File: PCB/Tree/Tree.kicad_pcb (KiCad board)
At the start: 2 copper layers, 70 x 98 mm, 36 parts, among them U1 HT16K33-28SOP

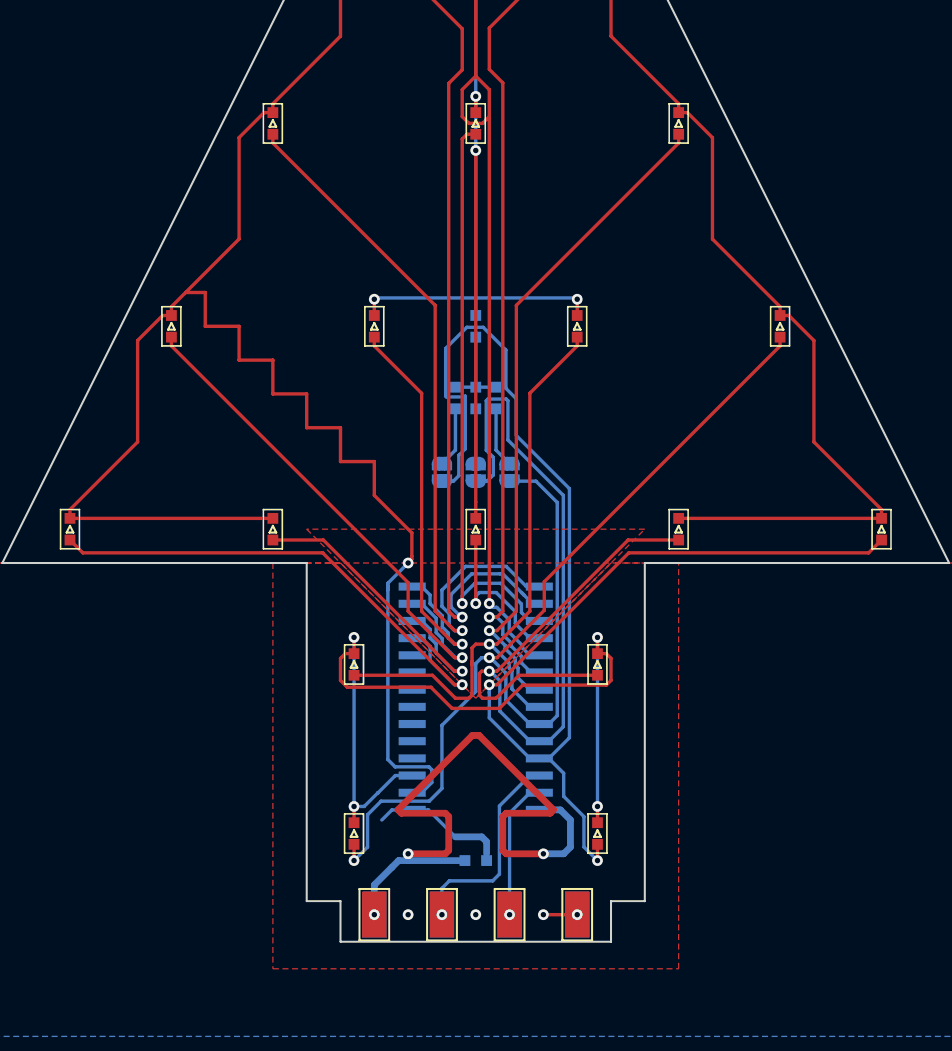
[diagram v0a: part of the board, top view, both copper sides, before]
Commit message: [update] Treeのコネクタ変更に伴う外形検討前 #2
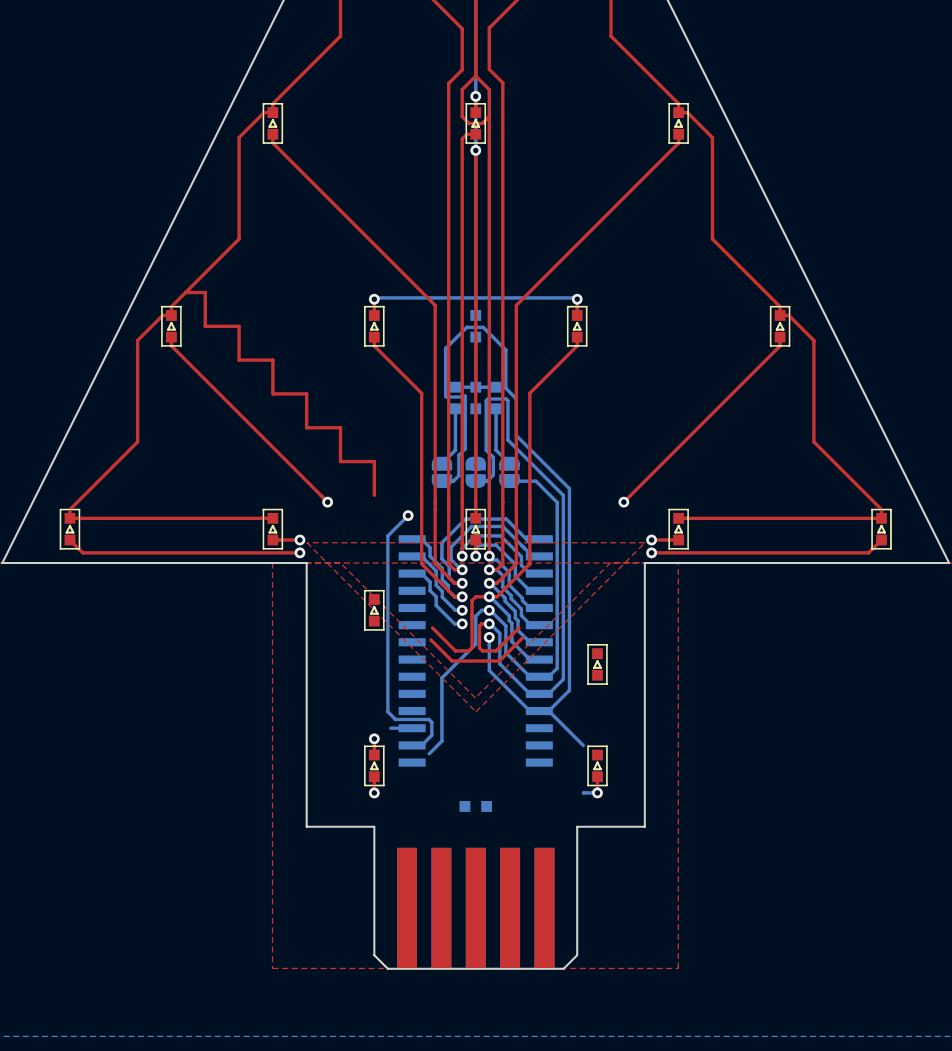
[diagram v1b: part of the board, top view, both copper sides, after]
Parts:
- removed TP1, TP2, TP3, TP4, TP5, TP6, TP7, TP8: TestPoint, TestPoint:TestPoint_Keystone_5015_Micro-Minature
- added J1: Conn_01x05, extsui:EDAC_5P_P2.54mm, F.Cu at (130.0, 150.5)
- D1, D10, D11, D12, D13, D14, D15, D16, D17, D18, D19, D2, D3, D4, D5, D6, D7, D8, D9: value GLED -> LED
- moved D18 5.22 mm to (122.5, 140.0)
- moved D16 5.00 mm to (139.0, 140.0)
- moved D19 4.27 mm to (122.5, 128.5)
- moved C1 4.00 mm to (130.0, 143.0)
- moved U1 3.50 mm to (130.0, 131.5)
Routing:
- net +5V: track 52.1 -> 0.00 mm, vias 3 -> 0
- net Net-(D16-Pad1): track 62.3 -> 10.9 mm, vias 4 -> 1
- net Net-(D18-Pad2): track 84.1 -> 55.9 mm, vias 2 -> 3
- net Net-(D17-Pad2): track 74.0 -> 48.7 mm, vias 1 -> 2
- net Net-(D1-Pad2): track 103.6 -> 79.7 mm, vias 2 -> 3
- net Net-(D15-Pad2): track 39.2 -> 17.4 mm
- net Net-(D14-Pad2): track 24.0 -> 7.99 mm, vias 1 -> 2
- net SCL: track 15.6 -> 0.00 mm, vias 1 -> 0
- net Net-(D13-Pad2): track 39.2 -> 23.9 mm, vias 1 -> 2
- net GND: track 12.4 -> 0.00 mm, vias 4 -> 0
- net SDA: track 11.3 -> 0.00 mm, vias 1 -> 0
- net Net-(D19-Pad2): track 47.0 -> 37.7 mm
- net Net-(D1-Pad1): track 328.2 -> 320.9 mm
- net Net-(D7-Pad2): track 76.7 -> 73.2 mm
- net Net-(D12-Pad2): track 32.3 -> 28.8 mm
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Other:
- board size 70 x 98 mm -> 70 x 100 mm
- board text removed: "GND"
- board text removed: "SCL"
- board text removed: "SDA"
- board text removed: "VCC"

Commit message: [update] Treeのコネクタ変更完了 #2
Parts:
- moved C1 4.61 mm to (125.5, 142.0), turned to 180 degrees
- moved D1 4.47 mm to (158.0, 118.5)
- moved D15 4.47 mm to (102.0, 118.5)
- moved D17 4.27 mm to (137.5, 128.5), turned to 90 degrees
- moved D14 4.00 mm to (115.0, 118.5)
- moved D2 4.00 mm to (145.0, 118.5)
- moved D8 4.00 mm to (130.0, 118.5)
- moved D13 3.35 mm to (109.0, 104.5)
- moved D3 3.35 mm to (151.0, 104.5)
- moved D12 3.00 mm to (122.5, 104.5)
- moved D4 3.00 mm to (137.5, 104.5)
- moved D11 2.24 mm to (116.0, 90.5)
- moved D5 2.24 mm to (144.0, 90.5)
- moved D9 2.00 mm to (130.0, 90.5)
- moved D16 1.50 mm to (137.5, 140.0)
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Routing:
- net GND: track 0.00 -> 41.7 mm, vias 0 -> 2
- net Net-(D16-Pad1): track 10.9 -> 42.5 mm
- net SCL: track 0.00 -> 27.5 mm, vias 0 -> 1
- net Net-(D1-Pad1): track 320.9 -> 293.6 mm
- net SDA: track 0.00 -> 26.6 mm, vias 0 -> 1
- net +5V: track 0.00 -> 24.0 mm, vias 0 -> 1
- net Net-(D17-Pad2): track 48.7 -> 71.9 mm, vias 2 -> 1
- net Net-(D18-Pad2): track 55.9 -> 79.0 mm, vias 3 -> 2
- net Net-(D15-Pad2): track 17.4 -> 39.8 mm
- net Net-(D1-Pad2): track 79.7 -> 99.7 mm, vias 3 -> 2
- net Net-(D14-Pad2): track 7.99 -> 26.3 mm, vias 2 -> 1
- net Net-(D13-Pad2): track 23.9 -> 38.5 mm, vias 2 -> 1
- net Net-(D19-Pad2): track 37.7 -> 45.9 mm
- net Net-(D8-Pad2): track 8.48 -> 12.5 mm
- net Net-(D12-Pad2): track 28.8 -> 31.8 mm
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- removed copper zone on F.Cu, net GND
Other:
- board size 70 x 100 mm -> 67.5 x 100 mm

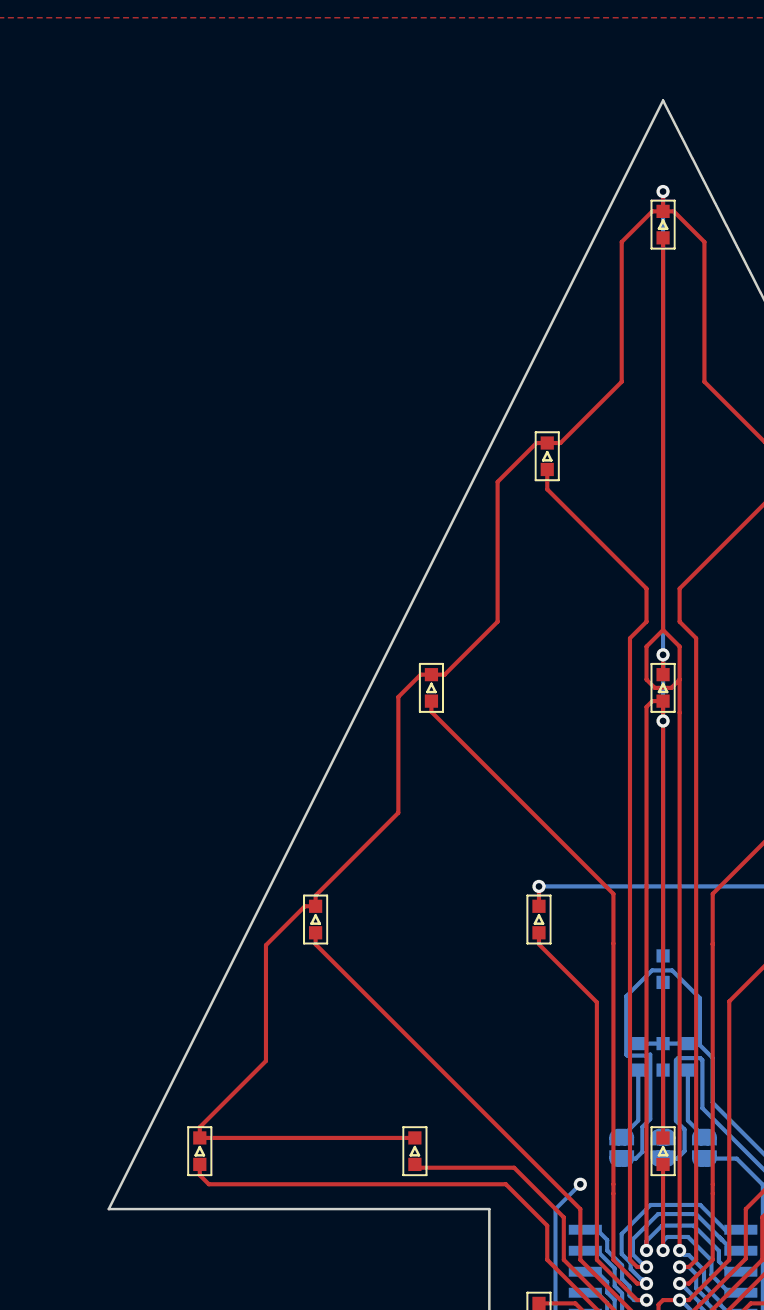
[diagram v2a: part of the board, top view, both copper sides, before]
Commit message: [update] Treeの左右で幅が異なっていたのを修正 #2
* 中心から右が34mm、左が33.5mmだったのを34mmに統一
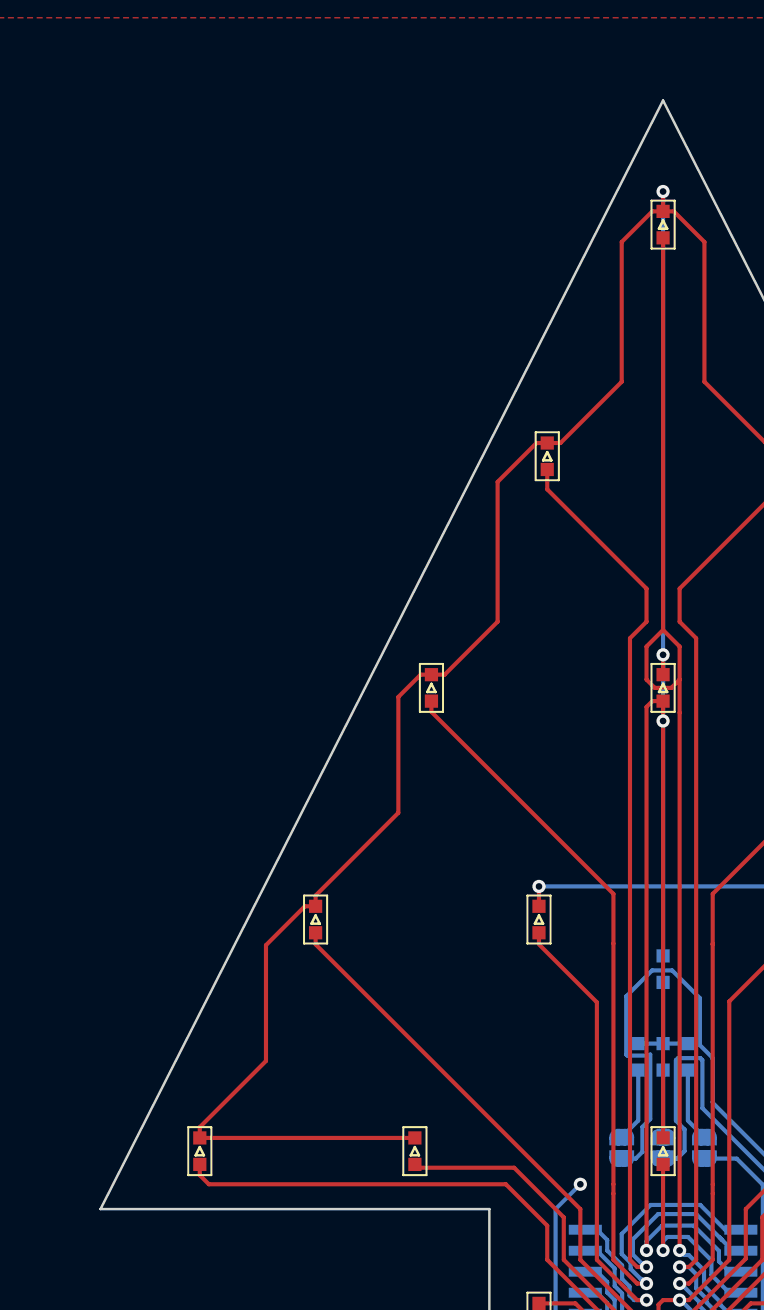
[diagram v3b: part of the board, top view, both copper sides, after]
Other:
- board size 67.5 x 100 mm -> 68 x 100 mm
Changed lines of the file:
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@@
   (general
     (thickness 1.6)
-    (drawings 17)
+    (drawings 19)
     (tracks 446)
     (zones 0)
@@
     )
   )
+  (dimension 34 (width 0.3) (layer F.CrtYd)
+    (gr_text "34.000 mm" (at 147 159.9) (layer F.CrtYd)
+      (effects (font (size 1.5 1.5) (thickness 0.3)))
+    )
+    (feature1 (pts (xy 130 162) (xy 130 161.413579)))
+    (feature2 (pts (xy 164 162) (xy 164 161.413579)))
+    (crossbar (pts (xy 164 162) (xy 130 162)))
+    (arrow1a (pts (xy 130 162) (xy 131.126504 161.413579)))
+    (arrow1b (pts (xy 130 162) (xy 131.126504 162.586421)))
+    (arrow2a (pts (xy 164 162) (xy 162.873496 161.413579)))
+    (arrow2b (pts (xy 164 162) (xy 162.873496 162.586421)))
+  )
+  (dimension 68 (width 0.3) (layer F.CrtYd)
+    (gr_text "68.000 mm" (at 130 165.9) (layer F.CrtYd)
+      (effects (font (size 1.5 1.5) (thickness 0.3)))
+    )
+    (feature1 (pts (xy 96 169) (xy 96 167.413579)))
+    (feature2 (pts (xy 164 169) (xy 164 167.413579)))
+    (crossbar (pts (xy 164 168) (xy 96 168)))
+    (arrow1a (pts (xy 96 168) (xy 97.126504 167.413579)))
+    (arrow1b (pts (xy 96 168) (xy 97.126504 168.586421)))
+    (arrow2a (pts (xy 164 168) (xy 162.873496 167.413579)))
+    (arrow2b (pts (xy 164 168) (xy 162.873496 168.586421)))
+  )
+  (dimension 34 (width 0.3) (layer F.CrtYd)
+    (gr_text "34.000 mm" (at 113 159.9) (layer F.CrtYd)
+      (effects (font (size 1.5 1.5) (thickness 0.3)))
+    )
+    (feature1 (pts (xy 96 162) (xy 96 161.413579)))
+    (feature2 (pts (xy 130 162) (xy 130 161.413579)))
+    (crossbar (pts (xy 130 162) (xy 96 162)))
+    (arrow1a (pts (xy 96 162) (xy 97.126504 161.413579)))
+    (arrow1b (pts (xy 96 162) (xy 97.126504 162.586421)))
+    (arrow2a (pts (xy 130 162) (xy 128.873496 161.413579)))
+    (arrow2b (pts (xy 130 162) (xy 128.873496 162.586421)))
+  )
   (gr_line (start 136.5 155) (end 137.5 154) (layer Edge.Cuts) (width 0.15))
   (gr_line (start 122.5 154) (end 123.5 155) (layer Edge.Cuts) (width 0.15))
@@
     (arrow2b (pts (xy 184.000001 55) (xy 184.586422 56.126504)))
   )
-  (dimension 70 (width 0.3) (layer F.Fab)
-    (gr_text "70.000 mm" (at 130 165.1) (layer F.Fab)
-      (effects (font (size 1.5 1.5) (thickness 0.3)))
-    )
-    (feature1 (pts (xy 165 162.5) (xy 165 163.586421)))
-    (feature2 (pts (xy 95 162.5) (xy 95 163.586421)))
-    (crossbar (pts (xy 95 163) (xy 165 163)))
-    (arrow1a (pts (xy 165 163) (xy 163.873496 163.586421)))
-    (arrow1b (pts (xy 165 163) (xy 163.873496 162.413579)))
-    (arrow2a (pts (xy 95 163) (xy 96.126504 163.586421)))
-    (arrow2b (pts (xy 95 163) (xy 96.126504 162.413579)))
-  )
   (gr_text "@ext_sui 2019.02\n" (at 130 99) (layer B.SilkS)
     (effects (font (size 1 1) (thickness 0.2) italic) (justify mirror))
   )
-  (gr_line (start 96.5 122) (end 130 55) (layer Edge.Cuts) (width 0.15))
+  (gr_line (start 96 122) (end 130 55) (layer Edge.Cuts) (width 0.15))
   (gr_line (start 130 55) (end 164 122) (layer Edge.Cuts) (width 0.15))
   (gr_line (start 164 122) (end 140.5 122) (layer Edge.Cuts) (width 0.15))
-  (gr_line (start 96.5 122) (end 119.5 122) (layer Edge.Cuts) (width 0.15))
+  (gr_line (start 96 122) (end 119.5 122) (layer Edge.Cuts) (width 0.15))
   (gr_line (start 119.5 144.5) (end 119.5 122) (layer Edge.Cuts) (width 0.15))
   (gr_line (start 140.5 144.5) (end 140.5 122) (layer Edge.Cuts) (width 0.15))

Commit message: [update] Tree v2.0登録 #2
* Tree v1.0 --> v2.0
* 作成日付も合わせて更新
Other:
- board text added: "@ext_sui 2020.04"
- board text added: "Tree Growing v2.0"
- board text removed: "@ext_sui 2019.02"
- board text removed: "Tree Growing v1.0"
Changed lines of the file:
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@@
     (arrow2b (pts (xy 184.000001 55) (xy 184.586422 56.126504)))
   )
-  (gr_text "@ext_sui 2019.02\n" (at 130 99) (layer B.SilkS)
+  (gr_text "@ext_sui 2020.04" (at 130 99) (layer B.SilkS)
     (effects (font (size 1 1) (thickness 0.2) italic) (justify mirror))
   )
@@
   (gr_line (start 122.5 144.5) (end 119.5 144.5) (layer Edge.Cuts) (width 0.15))
   (gr_line (start 137.5 144.5) (end 140.5 144.5) (layer Edge.Cuts) (width 0.15))
-  (gr_text "Tree Growing v1.0" (at 130 96.5) (layer B.SilkS)
+  (gr_text "Tree Growing v2.0" (at 130 96.5) (layer B.SilkS)
     (effects (font (size 1 1) (thickness 0.25) italic) (justify mirror))
   )
